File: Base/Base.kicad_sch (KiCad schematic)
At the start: 20 parts, among them J1 USB_C_Receptacle_USB2.0_16P, J2 JST_battery, J3 JST_header, J4 JST_speaker, J5 JST_debug, J6 JST_debug, SW1 SW_power, U1 MCP73831-2-OT, U2 MAX98357A

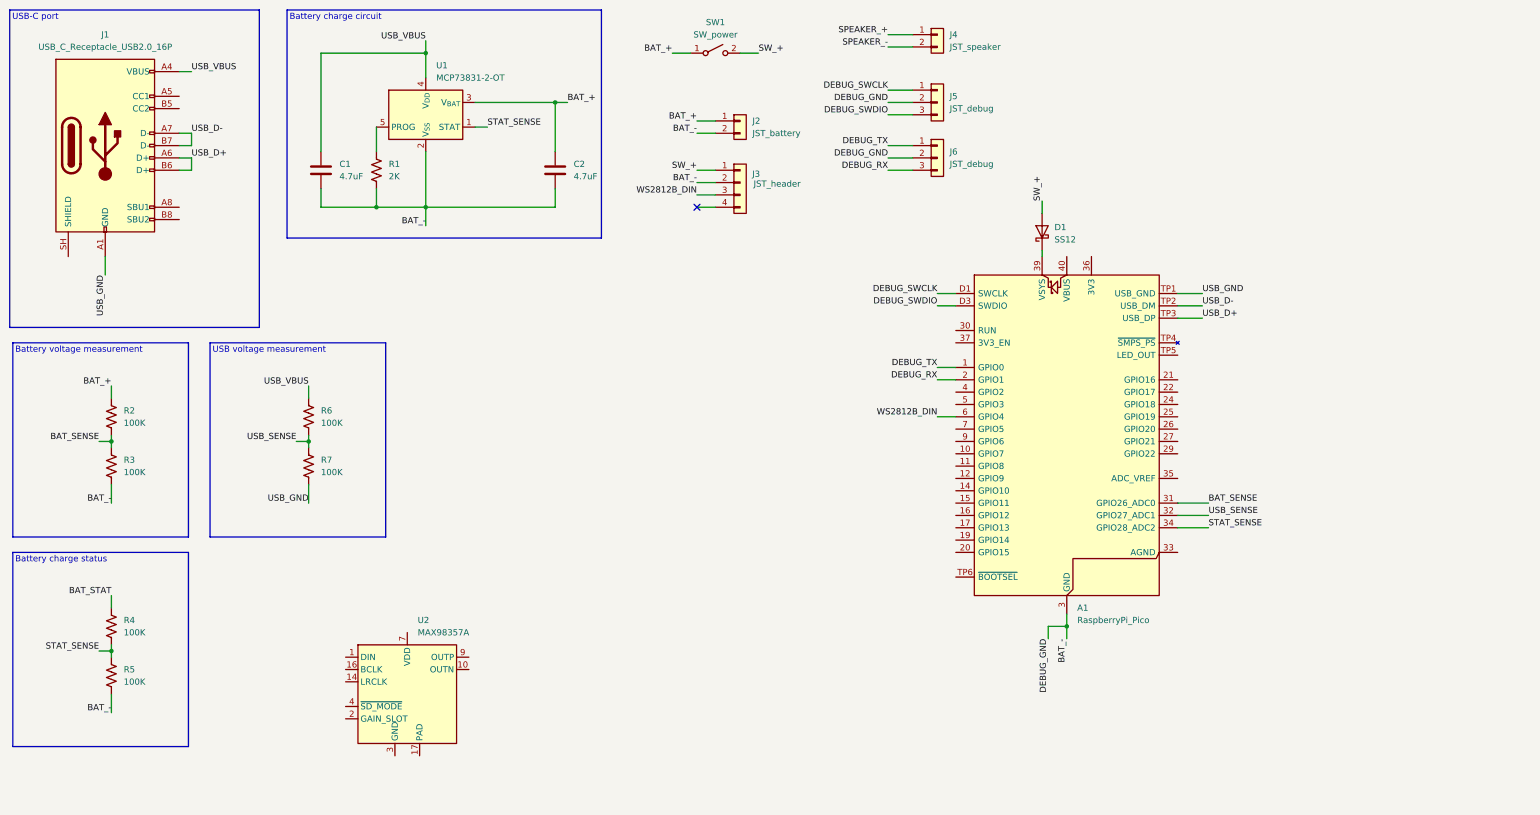
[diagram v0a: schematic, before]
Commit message: Add LED files, finish base and LED schematics
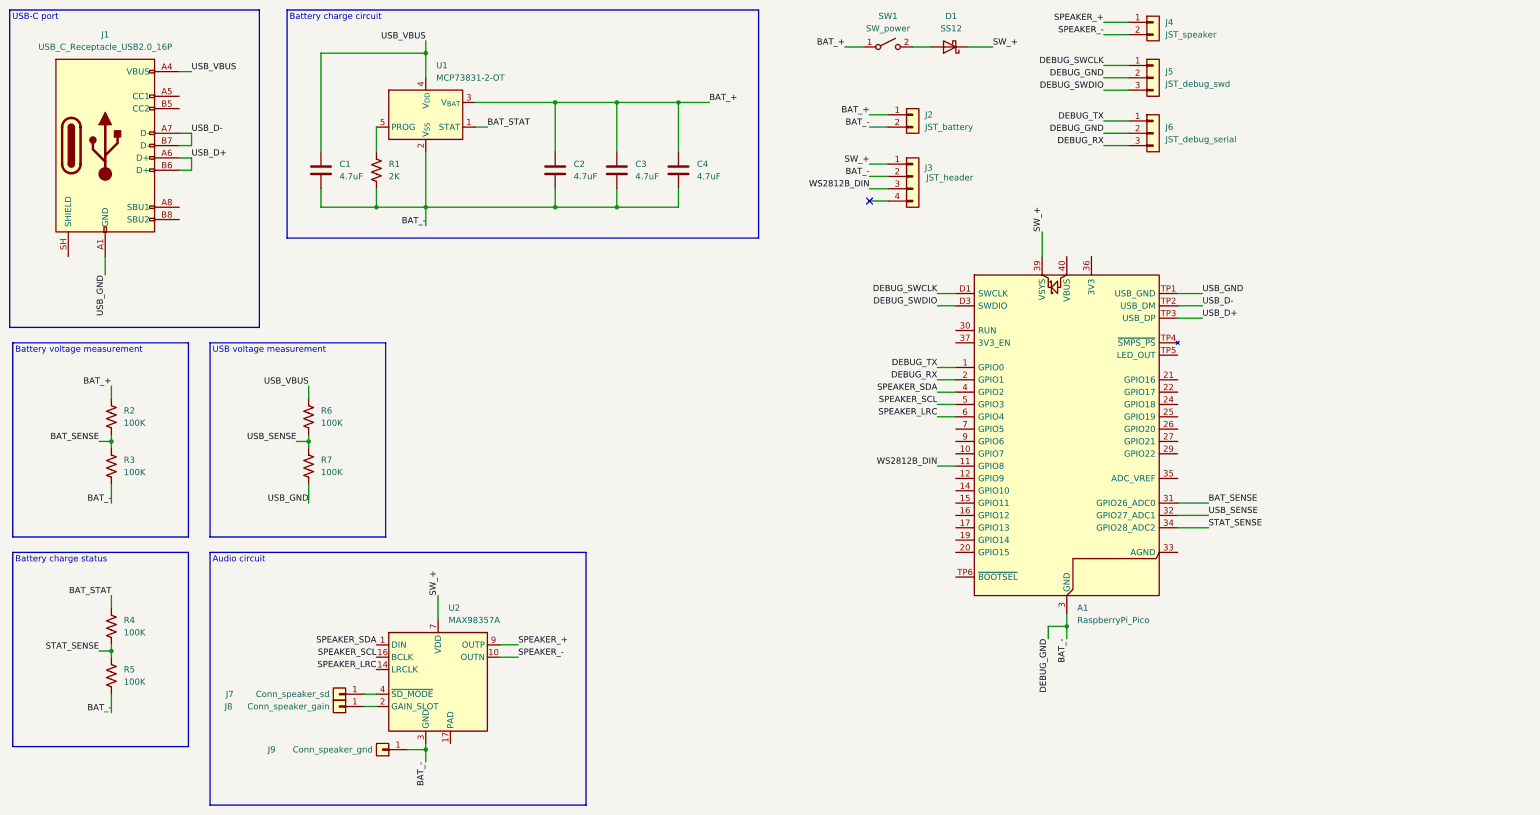
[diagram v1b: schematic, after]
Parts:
- added C3, C4: 4.7uF, Capacitor_SMD:C_0603_1608Metric_Pad1.08x0.95mm_HandSolder, symbol Device:C
- added J7: Conn_speaker_sd, TestPoint:TestPoint_THTPad_1.0x1.0mm_Drill0.5mm, symbol Connector_Generic:Conn_01x01
- added J8: Conn_speaker_gain, TestPoint:TestPoint_THTPad_1.0x1.0mm_Drill0.5mm, symbol Connector_Generic:Conn_01x01
- added J9: Conn_speaker_gnd, TestPoint:TestPoint_THTPad_1.0x1.0mm_Drill0.5mm, symbol Connector_Generic:Conn_01x01
- J5: value JST_debug -> JST_debug_swd
- J6: value JST_debug -> JST_debug_serial
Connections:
- net BAT_+: now also C3.2, C4.2
- net BAT_-: now also U2.11 (GND), U2.15 (GND), U2.3 (GND), C3.1, C4.1, J9.1 (Pin_1)
- net BAT_STAT: now also U1.1 (STAT)
- net SPEAKER_+: now also U2.9 (OUTP)
- net SPEAKER_-: now also U2.10 (OUTN)
- net STAT_SENSE: no longer U1.1 (STAT)
- net SW_+: now also A1.39 (VSYS), D1.1 (K), U2.7 (VDD), U2.8 (VDD); no longer D1.2 (A), SW1.2 (B)
- net WS2812B_DIN: now also A1.11 (GPIO8); no longer A1.6 (GPIO4)
- net SPEAKER_SDA: now reaches A1.4 (GPIO2)
- net SPEAKER_SDA: now also U2.1 (DIN)
- net SPEAKER_SCL: now reaches A1.5 (GPIO3)
- net SPEAKER_SCL: now also U2.16 (BCLK)
- net SPEAKER_LRC: now reaches U2.14 (LRCLK)
- net SPEAKER_LRC: now also A1.6 (GPIO4)
- net at U2.2 (GAIN_SLOT): now also J8.1 (Pin_1)
- net at U2.4 (~{SD_MODE}): now also J7.1 (Pin_1)
- new net: D1.2 (A), SW1.2 (B)
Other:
- note added: "Audio circuit"
- moved on the sheet: J2, J3, J4, J5, J6, SW1, U2

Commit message: Start work on PCBs, add CC resistors for USB charging
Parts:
- added R8, R9: 5.1k, Resistor_SMD:R_0603_1608Metric_Pad0.98x0.95mm_HandSolder, symbol Device:R_US
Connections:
- net USB_GND: now also R8.2, R9.2
- net at J1.A5 (CC1): now also R8.1
- net at J1.B5 (CC2): now also R9.1
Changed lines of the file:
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@@
+	)
+	(junction
+		(at 67.31 36.83)
+		(diameter 0)
+		(color 0 0 0 0)
 	)
 	(junction
@@
 	(wire
 		(pts
+			(xy 52.07 36.83) (xy 54.61 36.83)
+		)
+		(stroke
+			(width 0)
+			(type default)
+		)
+	)
+	(wire
+		(pts
 			(xy 242.57 21.59) (xy 247.65 21.59)
 		)
@@
 	(wire
 		(pts
+			(xy 52.07 34.29) (xy 54.61 34.29)
+		)
+		(stroke
+			(width 0)
+			(type default)
+		)
+	)
+	(wire
+		(pts
 			(xy 38.1 118.11) (xy 38.1 114.3)
 		)
@@
 	(wire
 		(pts
+			(xy 67.31 36.83) (xy 67.31 34.29)
+		)
+		(stroke
+			(width 0)
+			(type default)
+		)
+	)
+	(wire
+		(pts
 			(xy 242.57 39.37) (xy 247.65 39.37)
 		)
@@
 	(wire
 		(pts
+			(xy 67.31 39.37) (xy 67.31 36.83)
+		)
+		(stroke
+			(width 0)
+			(type default)
+		)
+	)
+	(wire
+		(pts
 			(xy 208.28 110.49) (xy 212.09 110.49)
 		)
@@
 	(wire
 		(pts
+			(xy 67.31 34.29) (xy 62.23 34.29)
+		)
+		(stroke
+			(width 0)
+			(type default)
+		)
+	)
+	(wire
+		(pts
 			(xy 154.94 57.15) (xy 142.24 57.15)
 		)
@@
 		(pts
 			(xy 90.17 157.48) (xy 92.71 157.48)
+		)
+		(stroke
+			(width 0)
+			(type default)
+		)
+	)
+	(wire
+		(pts
+			(xy 62.23 36.83) (xy 67.31 36.83)
 		)
 		(stroke
@@
 			)
 			(justify left bottom)
+		)
+	)
+	(label "USB_GND"
+		(at 67.31 39.37 270)
+		(effects
+			(font
+				(size 1.27 1.27)
+			)
+			(justify right bottom)
 		)
 	)
@@
 	)
 	(symbol
+		(lib_id "Device:R_US")
+		(at 58.42 36.83 90)
+		(unit 1)
+		(body_style 1)
+		(exclude_from_sim no)
+		(in_bom yes)
+		(on_board yes)
+		(in_pos_files yes)
+		(dnp no)
+		(property "Reference" "R9"
+			(at 54.61 35.814 90)
+			(show_name no)
+			(do_not_autoplace no)
+			(effects
+				(font
+					(size 1.27 1.27)
+				)
+			)
+		)
+		(property "Value" "5.1k"
+			(at 62.992 35.56 90)
+			(show_name no)
+			(do_not_autoplace no)
+			(effects
+				(font
+					(size 1.27 1.27)
+				)
+			)
+		)
+		(property "Footprint" "Resistor_SMD:R_0603_1608Metric_Pad0.98x0.95mm_HandSolder"
+			(at 58.674 35.814 90)
+			(hide yes)
+			(show_name no)
+			(do_not_autoplace no)
+			(effects
+				(font
+					(size 1.27 1.27)
+				)
+			)
+		)
+		(property "Datasheet" ""
+			(at 58.42 36.83 0)
+			(hide yes)
+			(show_name no)
+			(do_not_autoplace no)
+			(effects
+				(font
+					(size 1.27 1.27)
+				)
+			)
+		)
+		(property "Description" "Resistor, US symbol"
+			(at 58.42 36.83 0)
+			(hide yes)
+			(show_name no)
+			(do_not_autoplace no)
+			(effects
+				(font
+					(size 1.27 1.27)
+				)
+			)
+		)
+		(pin "1"
+		)
+		(pin "2"
+		)
+		(instances
+			(project "Base"
+				(path "/86209ff5-e3e5-4edf-9087-a19295ca511e"
+					(reference "R9")
+					(unit 1)
+				)
+			)
+		)
+	)
+	(symbol
 		(lib_id "Connector_Generic:Conn_01x03")
 		(at 252.73 41.91 0)
@@
 					(unit 1)
 				)
+			)
+		)
+	)
+	(symbol
+		(lib_id "Device:R_US")
+		(at 58.42 34.29 90)
+		(unit 1)
+		(body_style 1)
+		(exclude_from_sim no)
+		(in_bom yes)
+		(on_board yes)
+		(in_pos_files yes)
+		(dnp no)
+		(property "Reference" "R8"
+			(at 54.61 32.766 90)
+			(show_name no)
+			(do_not_autoplace no)
+			(effects
+				(font
+					(size 1.27 1.27)
+				)
+			)
+		)
+		(property "Value" "5.1k"
+			(at 62.992 32.766 90)
+			(show_name no)
+			(do_not_autoplace no)
+			(effects
+				(font
+					(size 1.27 1.27)
+				)
+			)
+		)
+		(property "Footprint" "Resistor_SMD:R_0603_1608Metric_Pad0.98x0.95mm_HandSolder"
+			(at 58.674 33.274 90)
+			(hide yes)
+			(show_name no)
+			(do_not_autoplace no)
+			(effects
+				(font
+					(size 1.27 1.27)
+				)
+			)
+		)
+		(property "Datasheet" ""
+			(at 58.42 34.29 0)
+			(hide yes)
+			(show_name no)
+			(do_not_autoplace no)
+			(effects
+				(font
+					(size 1.27 1.27)
+				)
+			)
+		)
+		(property "Description" "Resistor, US symbol"
+			(at 58.42 34.29 0)
+			(hide yes)
+			(show_name no)
+			(do_not_autoplace no)
+			(effects
+				(font
+					(size 1.27 1.27)
+				)
+			)
+		)
+		(pin "1"
+		)
+		(pin "2"
+		)
+		(instances
+			(project "Base"
+				(path "/86209ff5-e3e5-4edf-9087-a19295ca511e"
+					(reference "R8")
+					(unit 1)
+				)

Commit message: Almost finished routing the base PCB except USB
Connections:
- net USB_GND is gone; now on net BAT_-: A1.TP1 (USB_GND), J1.A1 (GND), J1.A12 (GND), J1.B1 (GND), J1.B12 (GND), R7.2, R8.2, R9.2
- net STAT_SENSE: now also A1.32 (GPIO27_ADC1); no longer A1.34 (GPIO28_ADC2)
- net USB_SENSE: now also A1.34 (GPIO28_ADC2); no longer A1.32 (GPIO27_ADC1)
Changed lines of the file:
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@@
+	)
+	(junction
+		(at 231.14 143.51)
+		(diameter 0)
+		(color 0 0 0 0)
 	)
 	(junction
@@
 	(wire
 		(pts
+			(xy 227.33 146.05) (xy 227.33 143.51)
+		)
+		(stroke
+			(width 0)
+			(type default)
+		)
+	)
+	(wire
+		(pts
 			(xy 264.16 123.19) (xy 257.81 123.19)
 		)
@@
 		(pts
 			(xy 38.1 105.41) (xy 38.1 106.68)
+		)
+		(stroke
+			(width 0)
+			(type default)
+		)
+	)
+	(wire
+		(pts
+			(xy 227.33 143.51) (xy 231.14 143.51)
 		)
 		(stroke
@@
 		)
 	)
-	(label "USB_SENSE"
-		(at 264.16 120.65 0)
-		(effects
-			(font
-				(size 1.27 1.27)
-			)
-			(justify left bottom)
-		)
-	)
 	(label "SPEAKER_-"
 		(at 242.57 21.59 180)
@@
 		)
 	)
+	(label "USB_SENSE"
+		(at 264.16 123.19 0)
+		(effects
+			(font
+				(size 1.27 1.27)
+			)
+			(justify left bottom)
+		)
+	)
 	(label "BAT_-"
 		(at 102.87 171.45 270)
@@
 		)
 	)
+	(label "USB_GND"
+		(at 227.33 146.05 270)
+		(effects
+			(font
+				(size 1.27 1.27)
+			)
+			(justify right bottom)
+		)
+	)
 	(label "USB_D-"
 		(at 54.61 41.91 0)
@@
 		)
 	)
-	(label "STAT_SENSE"
-		(at 264.16 123.19 0)
-		(effects
-			(font
-				(size 1.27 1.27)
-			)
-			(justify left bottom)
-		)
-	)
 	(label "USB_VBUS"
 		(at 54.61 29.21 0)
@@
 		)
 	)
+	(label "BAT_SENSE"
+		(at 264.16 118.11 0)
+		(effects
+			(font
+				(size 1.27 1.27)
+			)
+			(justify left bottom)
+		)
+	)
 	(label "SPEAKER_SCL"
 		(at 208.28 97.79 180)
@@
 		)
 	)
-	(label "BAT_SENSE"
-		(at 264.16 118.11 0)
-		(effects
-			(font
-				(size 1.27 1.27)
-			)
-			(justify left bottom)
-		)
-	)
 	(label "USB_GND"
 		(at 67.31 39.37 270)
@@
 		(effects
 			(font
+				(size 1.27 1.27)
+			)
+			(justify left bottom)
+		)
+	)
+	(label "STAT_SENSE"
+		(at 264.16 120.65 0)
+		(effects
+			(font

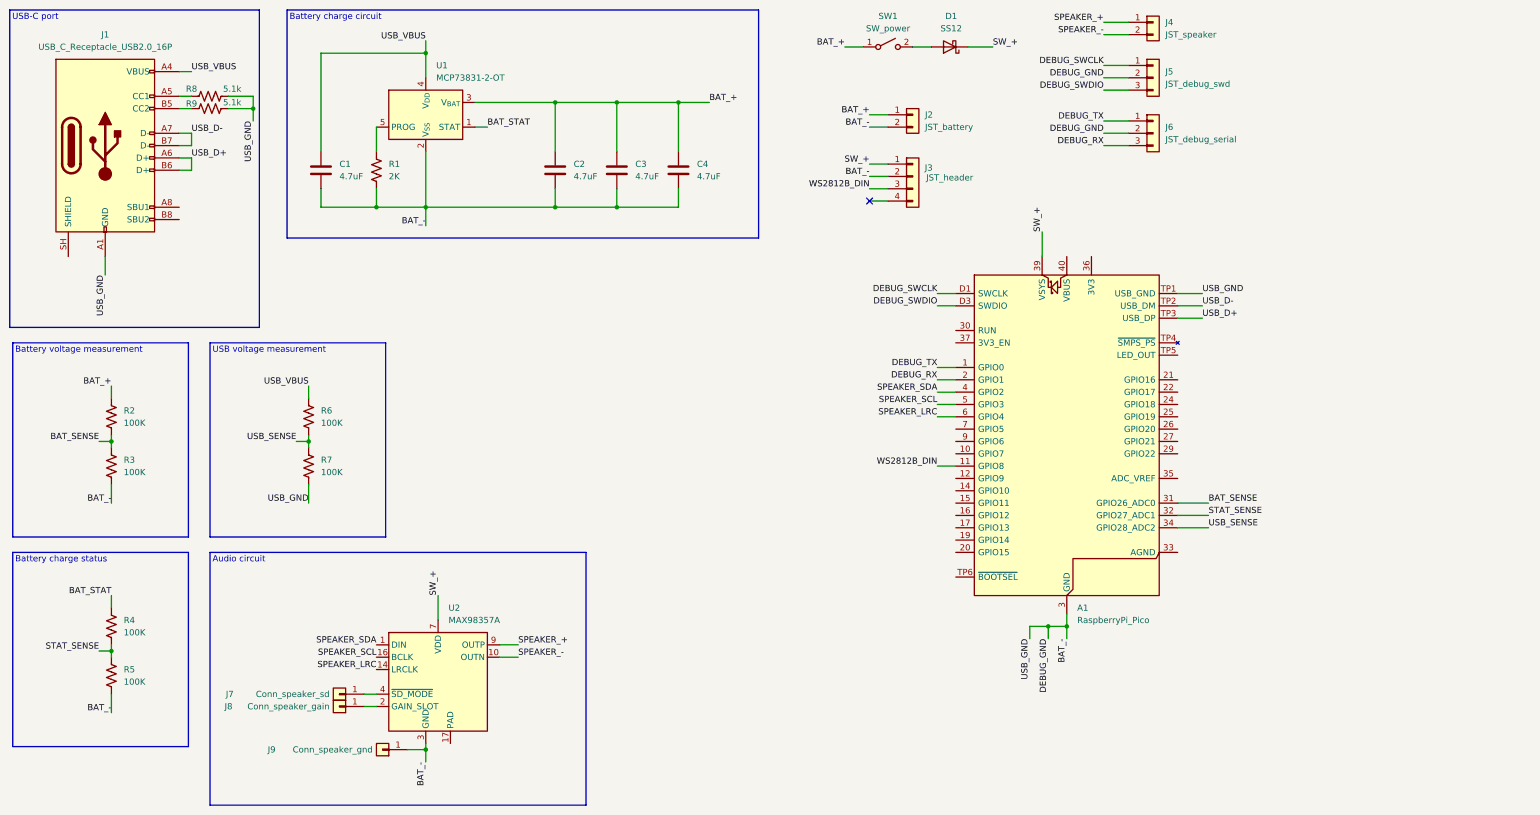
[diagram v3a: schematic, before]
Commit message: Update after DRC checks, add extra switches for mini hakkero
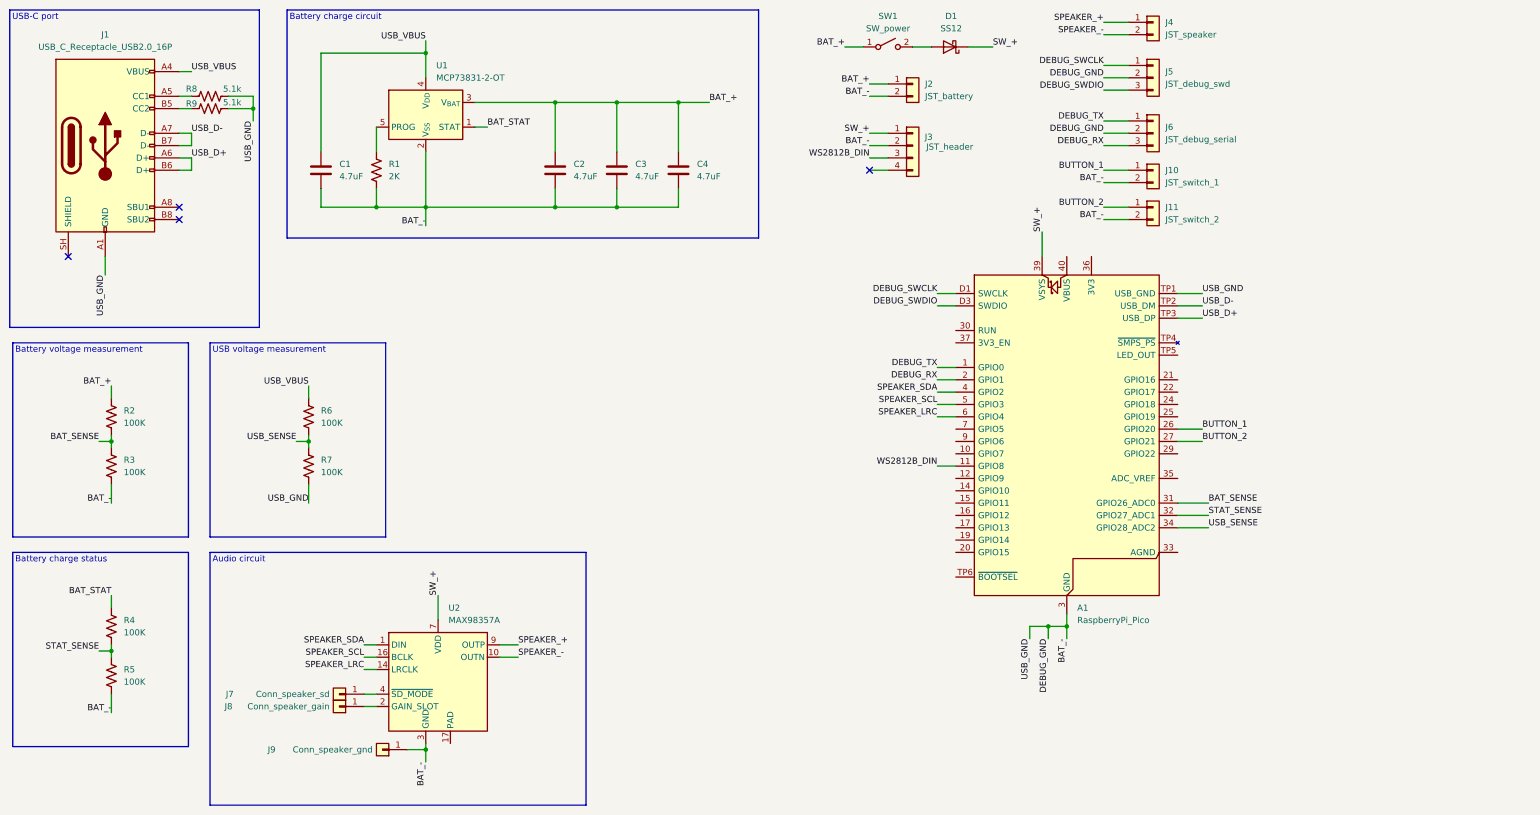
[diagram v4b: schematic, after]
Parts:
- added J10: JST_switch_1, Connector_JST:JST_SH_SM02B-SRSS-TB_1x02-1MP_P1.00mm_Horizontal, symbol Connector_Generic:Conn_01x02
- added J11: JST_switch_2, Connector_JST:JST_SH_SM02B-SRSS-TB_1x02-1MP_P1.00mm_Horizontal, symbol Connector_Generic:Conn_01x02
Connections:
- net BAT_-: now also J10.2 (Pin_2), J11.2 (Pin_2)
- net BUTTON_1: now reaches A1.26 (GPIO20)
- net BUTTON_1: now also J10.1 (Pin_1)
- net BUTTON_2: now reaches A1.27 (GPIO21)
- net BUTTON_2: now also J11.1 (Pin_1)
- no-connect marks 1 -> 4
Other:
- moved on the sheet: J2, J3

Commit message: Add touch pads for GPIO
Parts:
- added J12: Conn_touch_1, Connector_PinHeader_2.54mm:PinHeader_1x01_P2.54mm_Vertical, symbol Connector_Generic:Conn_01x01
- added J13: Conn_touch_2, Connector_PinHeader_2.54mm:PinHeader_1x01_P2.54mm_Vertical, symbol Connector_Generic:Conn_01x01
- added R10, R11: 1M, Resistor_SMD:R_0603_1608Metric_Pad0.98x0.95mm_HandSolder, symbol Device:R_US
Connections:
- net BAT_-: now also R10.2, R11.2
- net BUTTON_3: now reaches A1.16 (GPIO12)
- net BUTTON_3: now also J12.1 (Pin_1), R10.1
- net BUTTON_4: now reaches A1.17 (GPIO13)
- net BUTTON_4: now also J13.1 (Pin_1), R11.1
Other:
- note added: "Capacitive buttons"
